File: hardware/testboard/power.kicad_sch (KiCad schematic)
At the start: 8 parts, among them J701 Barrel_Jack, U702 AP2112K-1.2, U703 LT1084-3.3

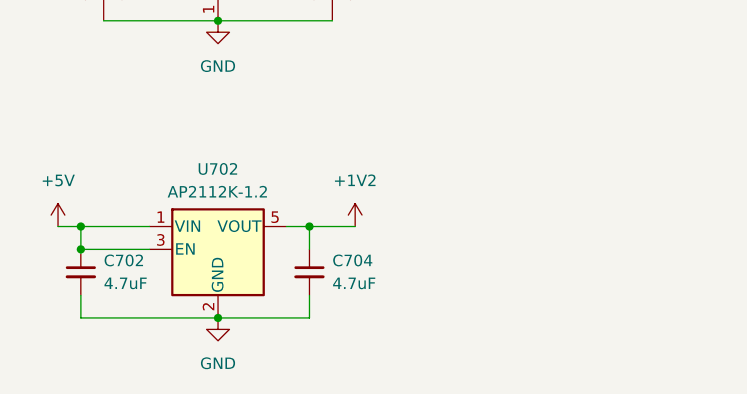
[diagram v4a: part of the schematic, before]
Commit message: layout FTDI
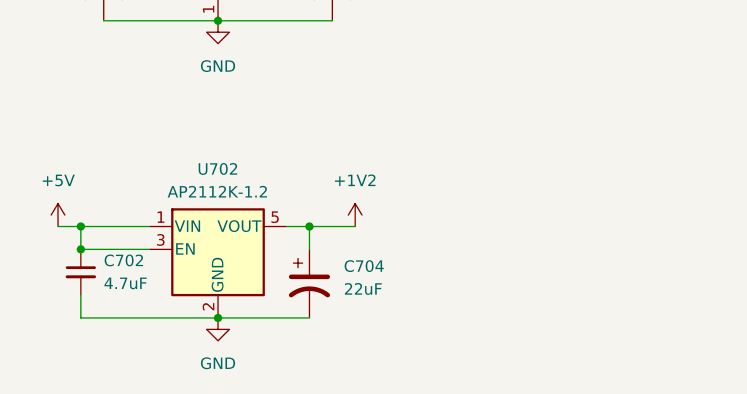
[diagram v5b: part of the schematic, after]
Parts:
- removed C704: 4.7uF, Capacitor_SMD:C_0603_1608Metric, symbol Device:C_Small
- added C704: 22uF, Capacitor_Tantalum_SMD:CP_EIA-2012-15_AVX-P, symbol Device:C_Polarized_US
- C706: footprint Capacitor_Tantalum_SMD:CP_EIA-2012-12_Kemet-R -> Capacitor_Tantalum_SMD:CP_EIA-2012-15_AVX-P
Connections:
- net +1V2: now also C704.1
- net GND: now also C704.2
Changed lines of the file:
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@@
-    (stroke (width 0) (type default))
-  )
-  (wire (pts (xy 73.66 162.56) (xy 73.66 165.1))
     (stroke (width 0) (type default))
   )
@@
       (effects (font (size 1.27 1.27)) (justify left))
     )
-    (property "Footprint" "Capacitor_Tantalum_SMD:CP_EIA-2012-12_Kemet-R" (at 76.2 128.27 0)
+    (property "Footprint" "Capacitor_Tantalum_SMD:CP_EIA-2012-15_AVX-P" (at 76.2 128.27 0)
       (effects (font (size 1.27 1.27)) hide)
     )
@@
     )
   )
-  (symbol (lib_id "Device:C_Small") (at 73.66 160.02 0) (unit 1)
-    (in_bom yes) (on_board yes) (dnp no) (fields_autoplaced)
-    (property "Reference" "C704" (at 76.2 158.7563 0)
-      (effects (font (size 1.27 1.27)) (justify left))
-    )
-    (property "Value" "4.7uF" (at 76.2 161.2963 0)
-      (effects (font (size 1.27 1.27)) (justify left))
-    )
-    (property "Footprint" "Capacitor_SMD:C_0603_1608Metric" (at 73.66 160.02 0)
-      (effects (font (size 1.27 1.27)) hide)
-    )
-    (property "Datasheet" "~" (at 73.66 160.02 0)
-      (effects (font (size 1.27 1.27)) hide)
-    )
-    (pin "2")
-    (pin "1")
+  (symbol (lib_id "Device:C_Small") (at 48.26 160.02 0) (unit 1)
+    (in_bom yes) (on_board yes) (dnp no) (fields_autoplaced)
+    (property "Reference" "C702" (at 50.8 158.7563 0)
+      (effects (font (size 1.27 1.27)) (justify left))
+    )
+    (property "Value" "4.7uF" (at 50.8 161.2963 0)
+      (effects (font (size 1.27 1.27)) (justify left))
+    )
+    (property "Footprint" "Capacitor_SMD:C_0603_1608Metric" (at 48.26 160.02 0)
+      (effects (font (size 1.27 1.27)) hide)
+    )
+    (property "Datasheet" "~" (at 48.26 160.02 0)
+      (effects (font (size 1.27 1.27)) hide)
+    )
+    (pin "2")
+    (pin "1")
+    (instances
+      (project "testboard"
+        (path "/a1ce156a-fb78-423b-b05a-d07384e5c8a7/6a2b0558-9bb2-48d3-955c-fa9d5ac4aef2"
+          (reference "C702") (unit 1)
+        )
+      )
+    )
+  )
+  (symbol (lib_id "power:PWR_FLAG") (at 119.38 81.28 0) (unit 1)
+    (in_bom yes) (on_board yes) (dnp no) (fields_autoplaced)
+    (property "Reference" "#FLG0701" (at 119.38 79.375 0)
+      (effects (font (size 1.27 1.27)) hide)
+    )
+    (property "Value" "PWR_FLAG" (at 119.38 76.2 0)
+      (effects (font (size 1.27 1.27)))
+    )
+    (property "Footprint" "" (at 119.38 81.28 0)
+      (effects (font (size 1.27 1.27)) hide)
+    )
+    (property "Datasheet" "~" (at 119.38 81.28 0)
+      (effects (font (size 1.27 1.27)) hide)
+    )
+    (pin "1")
+    (instances
+      (project "testboard"
+        (path "/a1ce156a-fb78-423b-b05a-d07384e5c8a7/6a2b0558-9bb2-48d3-955c-fa9d5ac4aef2"
+          (reference "#FLG0701") (unit 1)
+        )
+      )
+    )
+  )
+  (symbol (lib_id "power:+5V") (at 132.08 81.28 0) (unit 1)
+    (in_bom yes) (on_board yes) (dnp no) (fields_autoplaced)
+    (property "Reference" "#PWR0707" (at 132.08 85.09 0)
+      (effects (font (size 1.27 1.27)) hide)
+    )
+    (property "Value" "+5V" (at 132.08 76.2 0)
+      (effects (font (size 1.27 1.27)))
+    )
+    (property "Footprint" "" (at 132.08 81.28 0)
+      (effects (font (size 1.27 1.27)) hide)
+    )
+    (property "Datasheet" "" (at 132.08 81.28 0)
+      (effects (font (size 1.27 1.27)) hide)
+    )
+    (pin "1")
+    (instances
+      (project "testboard"
+        (path "/a1ce156a-fb78-423b-b05a-d07384e5c8a7/6a2b0558-9bb2-48d3-955c-fa9d5ac4aef2"
+          (reference "#PWR0707") (unit 1)
+        )
+      )
+    )
+  )
+  (symbol (lib_id "power:+5V") (at 45.72 154.94 0) (unit 1)
+    (in_bom yes) (on_board yes) (dnp no) (fields_autoplaced)
+    (property "Reference" "#PWR0702" (at 45.72 158.75 0)
+      (effects (font (size 1.27 1.27)) hide)
+    )
+    (property "Value" "+5V" (at 45.72 149.86 0)
+      (effects (font (size 1.27 1.27)))
+    )
+    (property "Footprint" "" (at 45.72 154.94 0)
+      (effects (font (size 1.27 1.27)) hide)
+    )
+    (property "Datasheet" "" (at 45.72 154.94 0)
+      (effects (font (size 1.27 1.27)) hide)
+    )
+    (pin "1")
+    (instances
+      (project "testboard"
+        (path "/a1ce156a-fb78-423b-b05a-d07384e5c8a7/6a2b0558-9bb2-48d3-955c-fa9d5ac4aef2"
+          (reference "#PWR0702") (unit 1)
+        )
+      )
+    )
+  )
+  (symbol (lib_id "power:+3.3V") (at 76.2 124.46 0) (unit 1)
+    (in_bom yes) (on_board yes) (dnp no) (fields_autoplaced)
+    (property "Reference" "#PWR0703" (at 76.2 128.27 0)
+      (effects (font (size 1.27 1.27)) hide)
+    )
+    (property "Value" "+3.3V" (at 76.2 119.38 0)
+      (effects (font (size 1.27 1.27)))
+    )
+    (property "Footprint" "" (at 76.2 124.46 0)
+      (effects (font (size 1.27 1.27)) hide)
+    )
+    (property "Datasheet" "" (at 76.2 124.46 0)
+      (effects (font (size 1.27 1.27)) hide)
+    )
+    (pin "1")
+    (instances
+      (project "testboard"
+        (path "/a1ce156a-fb78-423b-b05a-d07384e5c8a7/6a2b0558-9bb2-48d3-955c-fa9d5ac4aef2"
+          (reference "#PWR0703") (unit 1)
+        )
+      )
+    )
+  )
+  (symbol (lib_id "Device:C_Polarized_US") (at 73.66 161.29 0) (unit 1)
+    (in_bom yes) (on_board yes) (dnp no) (fields_autoplaced)
+    (property "Reference" "C704" (at 77.47 159.385 0)
+      (effects (font (size 1.27 1.27)) (justify left))
+    )
+    (property "Value" "22uF" (at 77.47 161.925 0)
+      (effects (font (size 1.27 1.27)) (justify left))
+    )
+    (property "Footprint" "Capacitor_Tantalum_SMD:CP_EIA-2012-15_AVX-P" (at 73.66 161.29 0)
+      (effects (font (size 1.27 1.27)) hide)
+    )
+    (property "Datasheet" "~" (at 73.66 161.29 0)
+      (effects (font (size 1.27 1.27)) hide)
+    )
+    (pin "1")
+    (pin "2")
     (instances
       (project "testboard"
@@
         )
       )
-    )
-  )
-  (symbol (lib_id "Device:C_Small") (at 48.26 160.02 0) (unit 1)
-    (in_bom yes) (on_board yes) (dnp no) (fields_autoplaced)
-    (property "Reference" "C702" (at 50.8 158.7563 0)
-      (effects (font (size 1.27 1.27)) (justify left))
-    )
-    (property "Value" "4.7uF" (at 50.8 161.2963 0)
-      (effects (font (size 1.27 1.27)) (justify left))
-    )
-    (property "Footprint" "Capacitor_SMD:C_0603_1608Metric" (at 48.26 160.02 0)
-      (effects (font (size 1.27 1.27)) hide)
-    )
-    (property "Datasheet" "~" (at 48.26 160.02 0)
-      (effects (font (size 1.27 1.27)) hide)
-    )
-    (pin "2")
-    (pin "1")
-    (instances
-      (project "testboard"
-        (path "/a1ce156a-fb78-423b-b05a-d07384e5c8a7/6a2b0558-9bb2-48d3-955c-fa9d5ac4aef2"
-          (reference "C702") (unit 1)
-        )
-      )
-    )
-  )
-  (symbol (lib_id "power:PWR_FLAG") (at 119.38 81.28 0) (unit 1)
-    (in_bom yes) (on_board yes) (dnp no) (fields_autoplaced)
-    (property "Reference" "#FLG0701" (at 119.38 79.375 0)
-      (effects (font (size 1.27 1.27)) hide)
-    )
-    (property "Value" "PWR_FLAG" (at 119.38 76.2 0)
-      (effects (font (size 1.27 1.27)))
-    )
-    (property "Footprint" "" (at 119.38 81.28 0)
-      (effects (font (size 1.27 1.27)) hide)
-    )
-    (property "Datasheet" "~" (at 119.38 81.28 0)
-      (effects (font (size 1.27 1.27)) hide)
-    )
-    (pin "1")
-    (instances
-      (project "testboard"
-        (path "/a1ce156a-fb78-423b-b05a-d07384e5c8a7/6a2b0558-9bb2-48d3-955c-fa9d5ac4aef2"
-          (reference "#FLG0701") (unit 1)
-        )
-      )
-    )
-  )
-  (symbol (lib_id "power:+5V") (at 132.08 81.28 0) (unit 1)
-    (in_bom yes) (on_board yes) (dnp no) (fields_autoplaced)
-    (property "Reference" "#PWR0707" (at 132.08 85.09 0)
-      (effects (font (size 1.27 1.27)) hide)
-    )
-    (property "Value" "+5V" (at 132.08 76.2 0)
-      (effects (font (size 1.27 1.27)))
-    )
-    (property "Footprint" "" (at 132.08 81.28 0)
-      (effects (font (size 1.27 1.27)) hide)
-    )
-    (property "Datasheet" "" (at 132.08 81.28 0)
-      (effects (font (size 1.27 1.27)) hide)
-    )
-    (pin "1")
-    (instances
-      (project "testboard"
-        (path "/a1ce156a-fb78-423b-b05a-d07384e5c8a7/6a2b0558-9bb2-48d3-955c-fa9d5ac4aef2"
-          (reference "#PWR0707") (unit 1)
-        )
-      )
-    )
-  )
-  (symbol (lib_id "power:+5V") (at 45.72 154.94 0) (unit 1)
-    (in_bom yes) (on_board yes) (dnp no) (fields_autoplaced)
-    (property "Reference" "#PWR0702" (at 45.72 158.75 0)
-      (effects (font (size 1.27 1.27)) hide)
-    )
-    (property "Value" "+5V" (at 45.72 149.86 0)
-      (effects (font (size 1.27 1.27)))
-    )
-    (property "Footprint" "" (at 45.72 154.94 0)
-      (effects (font (size 1.27 1.27)) hide)
-    )
-    (property "Datasheet" "" (at 45.72 154.94 0)
-      (effects (font (size 1.27 1.27)) hide)
-    )
-    (pin "1")
-    (instances
-      (project "testboard"
-        (path "/a1ce156a-fb78-423b-b05a-d07384e5c8a7/6a2b0558-9bb2-48d3-955c-fa9d5ac4aef2"
-          (reference "#PWR0702") (unit 1)
-        )
-      )
-    )
-  )
-  (symbol (lib_id "power:+3.3V") (at 76.2 124.46 0) (unit 1)
-    (in_bom yes) (on_board yes) (dnp no) (fields_autoplaced)
-    (property "Reference" "#PWR0703" (at 76.2 128.27 0)
-      (effects (font (size 1.27 1.27)) hide)
-    )
-    (property "Value" "+3.3V" (at 76.2 119.38 0)
-      (effects (font (size 1.27 1.27)))
-    )
-    (property "Footprint" "" (at 76.2 124.46 0)
-      (effects (font (size 1.27 1.27)) hide)
-    )
-    (property "Datasheet" "" (at 76.2 124.46 0)
-      (effects (font (size 1.27 1.27)) hide)
-    )
-    (pin "1")
-    (instances
-      (project "testboard"
-        (path "/a1ce156a-fb78-423b-b05a-d07384e5c8a7/6a2b0558-9bb2-48d3-955c-fa9d5ac4aef2"
-          (reference "#PWR0703") (unit 1)
-        )
-      )
